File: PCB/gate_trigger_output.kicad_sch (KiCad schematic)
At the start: 9 parts

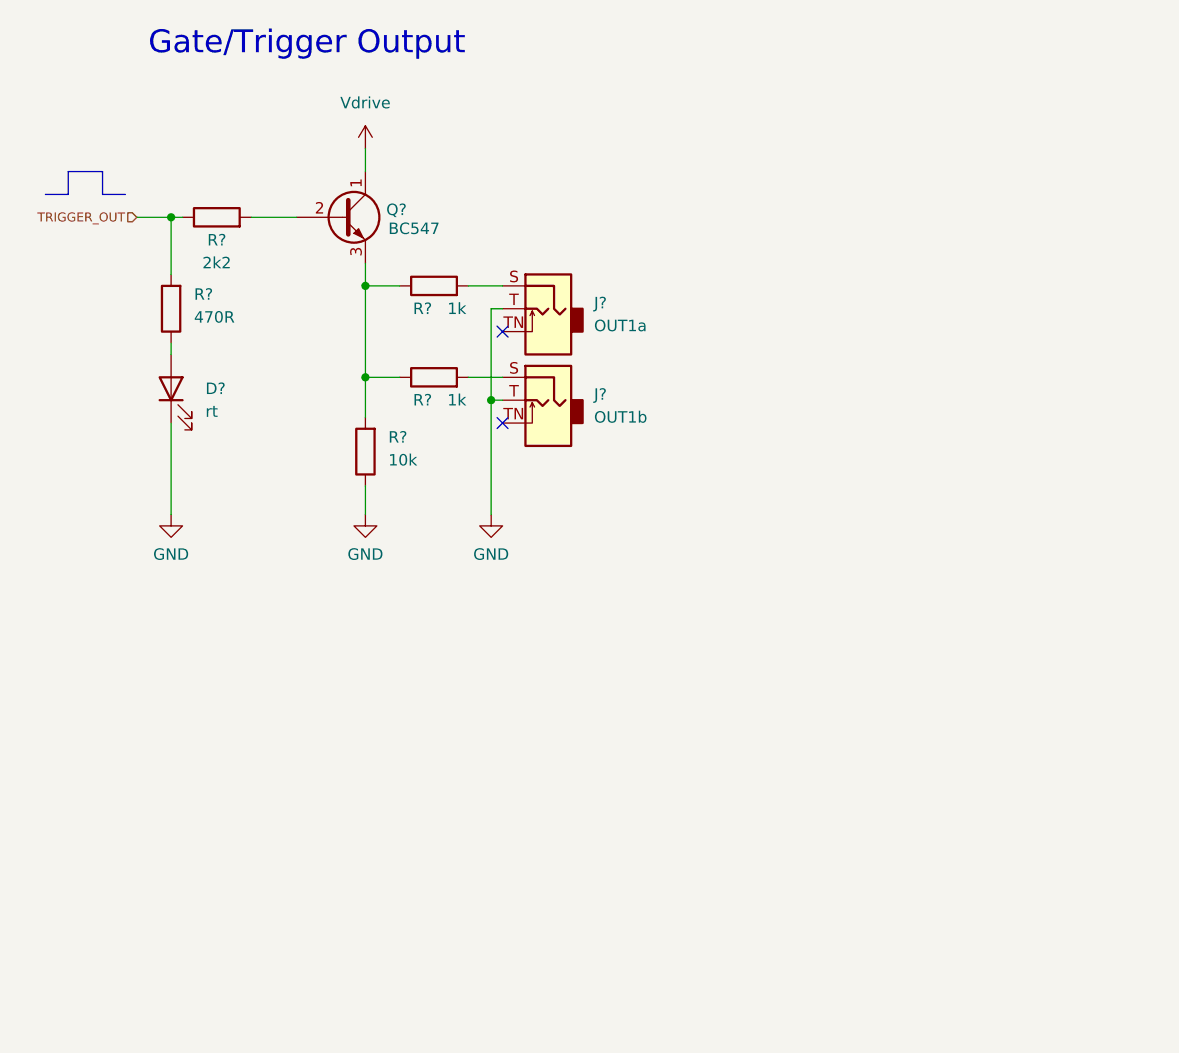
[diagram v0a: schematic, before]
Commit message: :art: Decompose schematic parts for the output
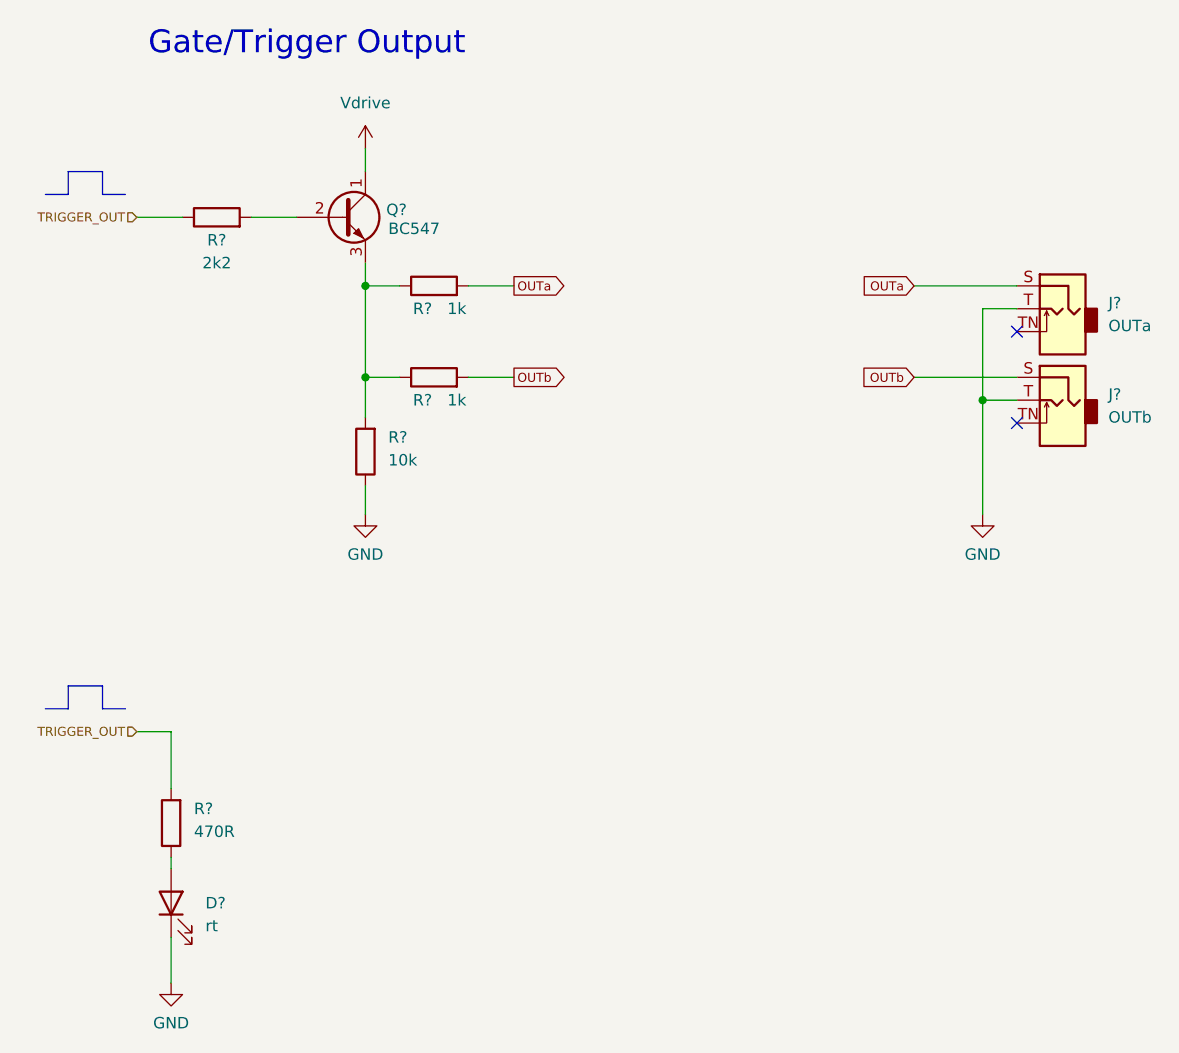
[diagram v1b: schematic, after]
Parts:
- removed D?: rt, symbol Device:LED
- removed R?: 470R, symbol Device:R
- added D?: rt, symbol Device:LED
- added R?: 470R, symbol Device:R
- J?: value OUT1a -> OUTa
- J?: value OUT1b -> OUTb
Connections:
- net GND: now also D?.1 (K)
- net TRIGGER_OUT: now also R?.2
- net OUTa: now reaches J?.S, R?.2
- net OUTb: now reaches J?.S, R?.2
- new net: D?.2 (A), R?.1
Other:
- moved on the sheet: J?

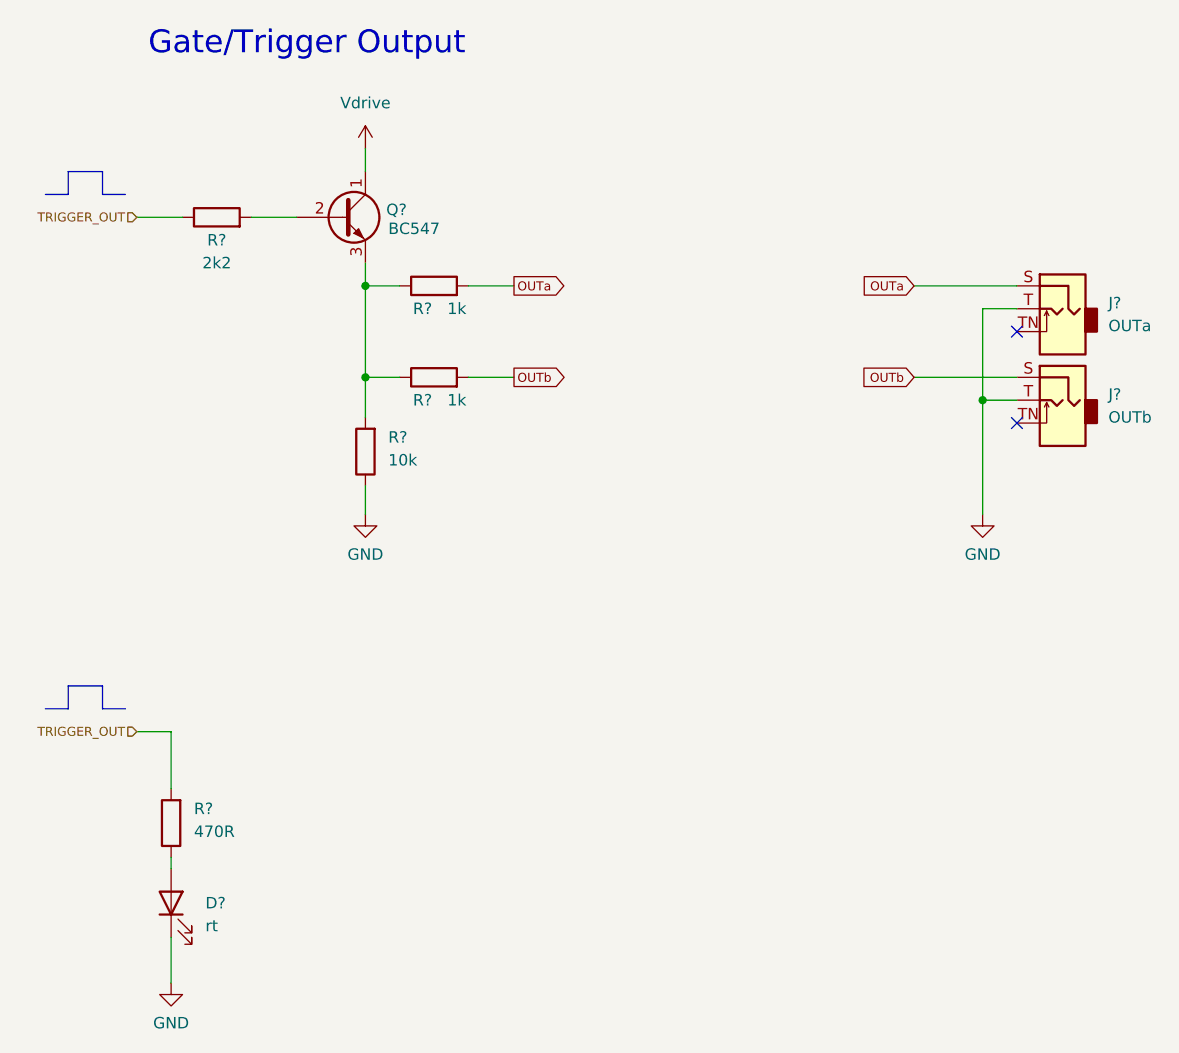
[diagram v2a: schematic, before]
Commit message: :wrench: Assign component designators
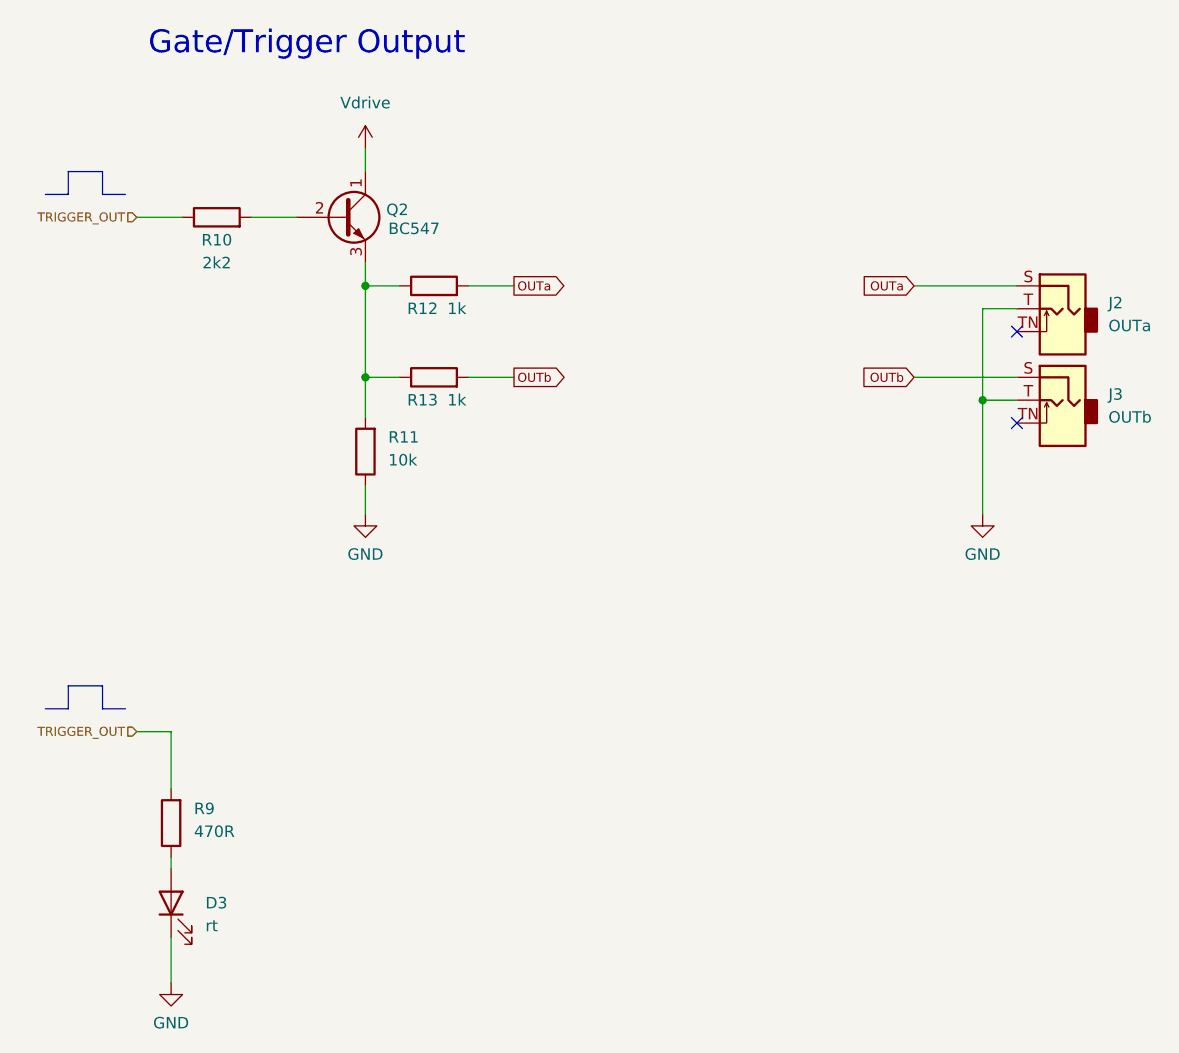
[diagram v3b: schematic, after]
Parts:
- gave numbers to parts that had none: 9

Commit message: :wrench: Assign footprints to all symbols
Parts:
- D3: footprint (none) -> LED_THT:LED_D3.0mm
- R10, R11, R12, R13, R9: footprint (none) -> Resistor_THT:R_Axial_DIN0207_L6.3mm_D2.5mm_P7.62mm_Horizontal
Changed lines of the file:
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@@
       (effects (font (size 1.27 1.27)) (justify right))
     )
-    (property "Footprint" "" (at 60.198 70.485 90)
+    (property "Footprint" "Resistor_THT:R_Axial_DIN0207_L6.3mm_D2.5mm_P7.62mm_Horizontal" (at 60.198 70.485 90)
       (effects (font (size 1.27 1.27)) hide)
     )
@@
       (effects (font (size 1.27 1.27)))
     )
-    (property "Footprint" "" (at 41.91 46.228 90)
+    (property "Footprint" "Resistor_THT:R_Axial_DIN0207_L6.3mm_D2.5mm_P7.62mm_Horizontal" (at 41.91 46.228 90)
       (effects (font (size 1.27 1.27)) hide)
     )
@@
       (effects (font (size 1.27 1.27)))
     )
-    (property "Footprint" "" (at 66.04 64.008 90)
+    (property "Footprint" "Resistor_THT:R_Axial_DIN0207_L6.3mm_D2.5mm_P7.62mm_Horizontal" (at 66.04 64.008 90)
       (effects (font (size 1.27 1.27)) hide)
     )
@@
       (effects (font (size 1.27 1.27)) (justify right))
     )
-    (property "Footprint" "" (at 38.608 111.76 90)
+    (property "Footprint" "Resistor_THT:R_Axial_DIN0207_L6.3mm_D2.5mm_P7.62mm_Horizontal" (at 38.608 111.76 90)
       (effects (font (size 1.27 1.27)) hide)
     )
@@
       (effects (font (size 1.27 1.27)) (justify right))
     )
-    (property "Footprint" "" (at 36.83 120.65 0)
+    (property "Footprint" "LED_THT:LED_D3.0mm" (at 36.83 120.65 0)
       (effects (font (size 1.27 1.27)) hide)
     )
@@
       (effects (font (size 1.27 1.27)))
     )
-    (property "Footprint" "" (at 66.04 53.848 90)
-      (effects (font (size 1.27 1.27)) hide)
-    )
+    (property "Footprint" "Resistor_THT:R_Axial_DIN0207_L6.3mm_D2.5mm_P7.62mm_Horizontal" (at 66.04 53.848 90)
+      (effects (font (size 1.27 1.27)) hide)
+    )

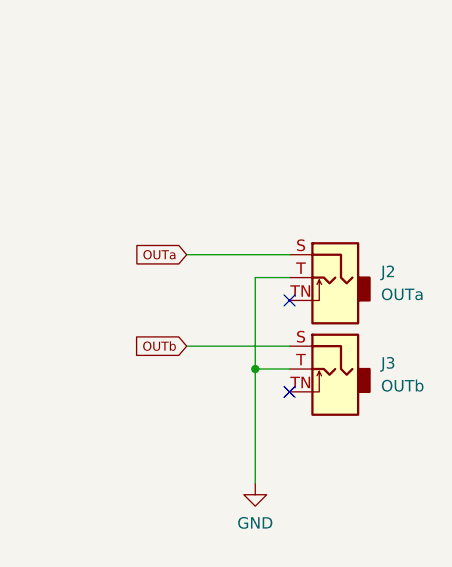
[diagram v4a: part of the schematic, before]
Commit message: :sparkles: Set PCB size and UI component placement
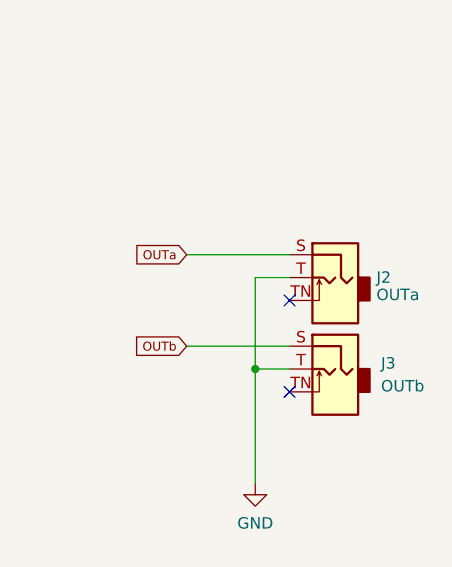
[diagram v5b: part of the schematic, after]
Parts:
- J2, J3: footprint Connector_Audio:Jack_3.5mm_QingPu_WQP-PJ398SM_Vertical_CircularHoles -> moPsy:Jack_3.5mm_QingPu_WQP-PJ398SM_Vertical_CircularHoles_Centered
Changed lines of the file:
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@@
   (symbol (lib_id "Connector:AudioJack2_Ground_SwitchT") (at 135.89 54.61 0) (mirror y) (unit 1)
     (in_bom yes) (on_board yes) (dnp no) (fields_autoplaced)
-    (property "Reference" "J2" (at 140.97 53.9749 0)
-      (effects (font (size 1.27 1.27)) (justify right))
-    )
-    (property "Value" "OUTa" (at 140.97 56.5149 0)
-      (effects (font (size 1.27 1.27)) (justify right))
-    )
-    (property "Footprint" "Connector_Audio:Jack_3.5mm_QingPu_WQP-PJ398SM_Vertical_CircularHoles" (at 135.89 54.61 0)
+    (property "Reference" "J2" (at 140.462 54.6013 0)
+      (effects (font (size 1.27 1.27)) (justify right))
+    )
+    (property "Value" "OUTa" (at 140.462 56.5223 0)
+      (effects (font (size 1.27 1.27)) (justify right))
+    )
+    (property "Footprint" "moPsy:Jack_3.5mm_QingPu_WQP-PJ398SM_Vertical_CircularHoles_Centered" (at 135.89 54.61 0)
       (effects (font (size 1.27 1.27)) hide)
     )
@@
       (effects (font (size 1.27 1.27)) (justify right))
     )
-    (property "Footprint" "Connector_Audio:Jack_3.5mm_QingPu_WQP-PJ398SM_Vertical_CircularHoles" (at 135.89 64.77 0)
-      (effects (font (size 1.27 1.27)) hide)
-    )
+    (property "Footprint" "moPsy:Jack_3.5mm_QingPu_WQP-PJ398SM_Vertical_CircularHoles_Centered" (at 135.89 64.77 0)
+      (effects (font (size 1.27 1.27)) hide)
+    )
